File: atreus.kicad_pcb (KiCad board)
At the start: 2 copper layers, 139.7 x 101.6 mm, 45 parts

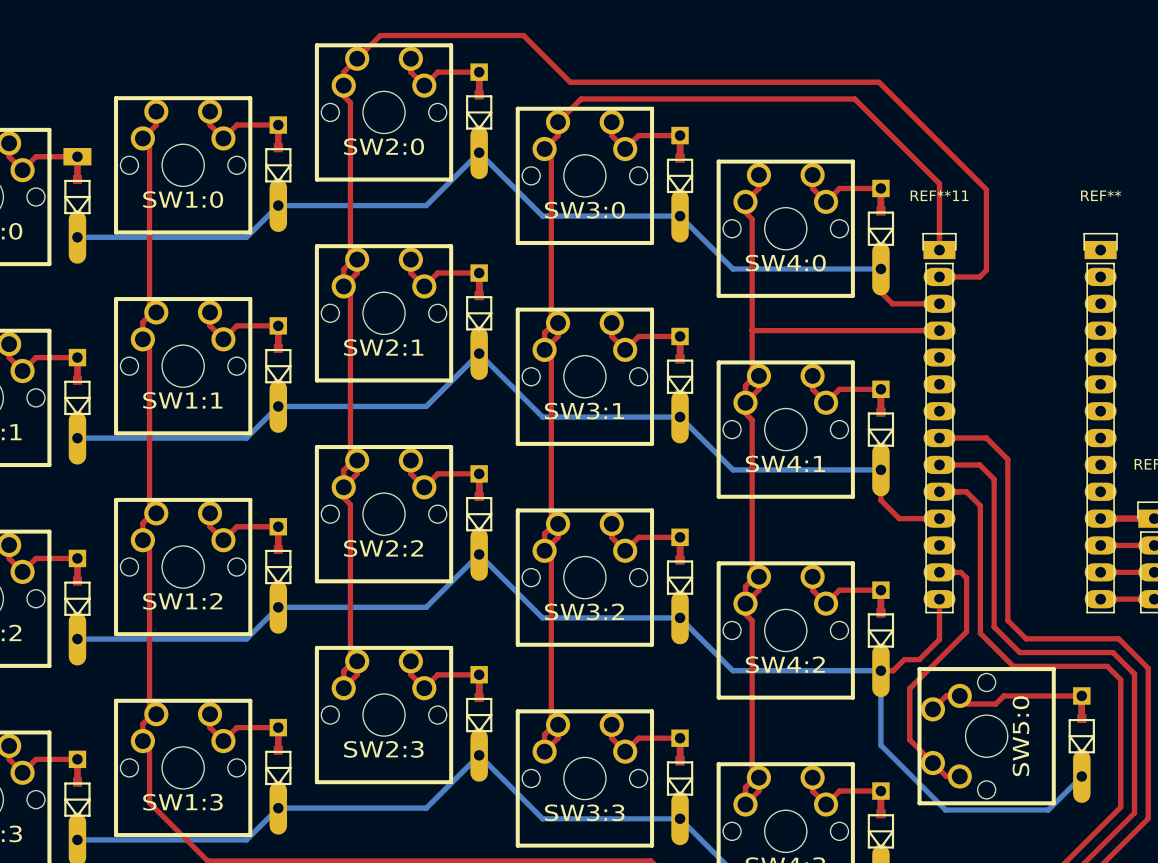
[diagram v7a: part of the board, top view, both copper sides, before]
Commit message: make diode pads bigger
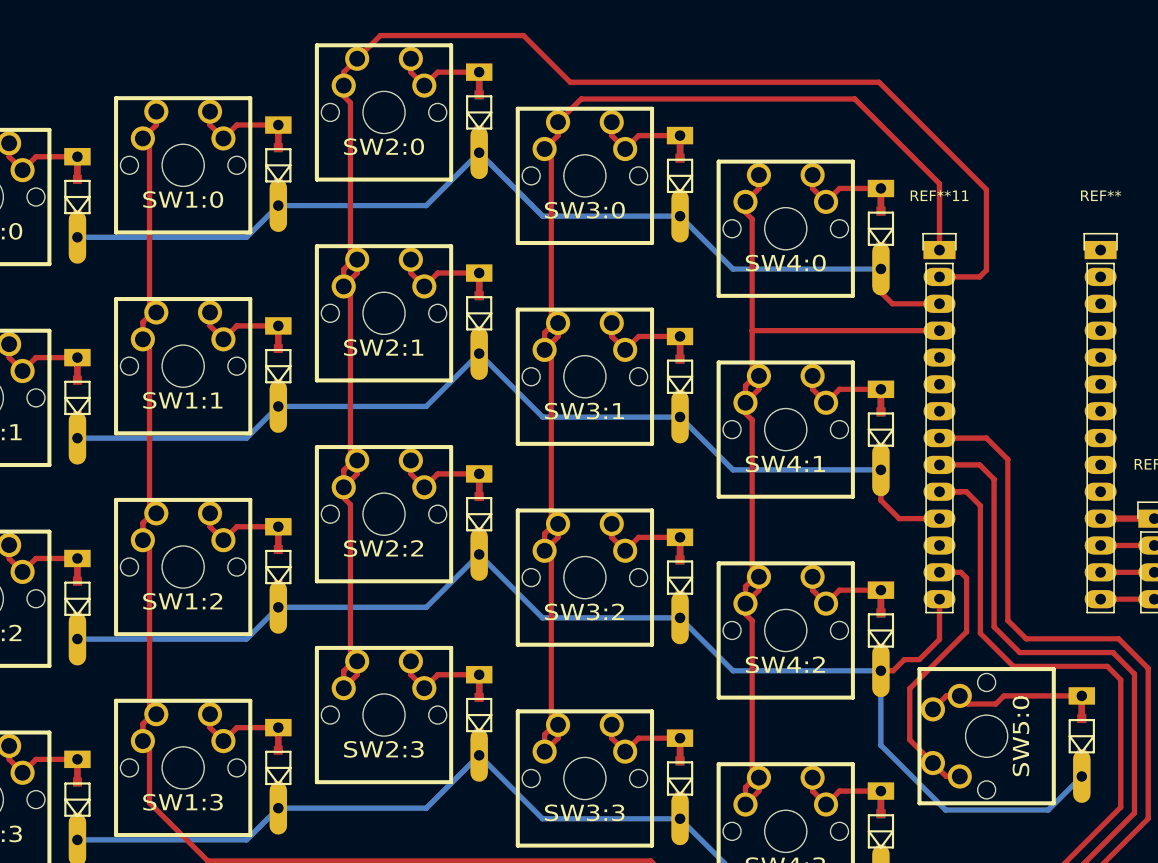
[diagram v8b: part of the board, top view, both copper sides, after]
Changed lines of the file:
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@@
     (mod_text_size 1.524 1.524)
     (mod_text_width 0.3048)
-    (pad_size 1.651 5)
+    (pad_size 2.5 1.651)
     (pad_drill 0.9906)
     (pad_to_mask_clearance 0.254)
@@
     (pad 1 thru_hole oval (at -3.81 0 180) (size 1.651 5) (drill 0.9906) (layers *.Cu *.SilkS *.Mask)
       (net 1 N-row-0))
-    (pad 2 thru_hole rect (at 3.81 0) (size 2.651 1.651) (drill 0.9906) (layers *.Cu *.SilkS *.Mask)
+    (pad 2 thru_hole rect (at 3.81 0) (size 2.5 1.651) (drill 0.9906) (layers *.Cu *.SilkS *.Mask)
       (net 11 N-diode-0))
     (pad 99 smd rect (at -1.6637 0) (size 0.8382 0.8382) (layers Front F.Paste F.Mask))
@@
     (pad 1 thru_hole oval (at -3.81 0 180) (size 1.651 5) (drill 0.9906) (layers *.Cu *.SilkS *.Mask)
       (net 2 N-row-1))
-    (pad 2 thru_hole rect (at 3.81 0) (size 1.651 1.651) (drill 0.9906) (layers *.Cu *.SilkS *.Mask)
+    (pad 2 thru_hole rect (at 3.81 0) (size 2.5 1.651) (drill 0.9906) (layers *.Cu *.SilkS *.Mask)
       (net 12 N-diode-1))
     (pad 99 smd rect (at -1.6637 0) (size 0.8382 0.8382) (layers Front F.Paste F.Mask))
@@
     (pad 1 thru_hole oval (at -3.81 0 180) (size 1.651 5) (drill 0.9906) (layers *.Cu *.SilkS *.Mask)
       (net 3 N-row-2))
-    (pad 2 thru_hole rect (at 3.81 0) (size 1.651 1.651) (drill 0.9906) (layers *.Cu *.SilkS *.Mask)
+    (pad 2 thru_hole rect (at 3.81 0) (size 2.5 1.651) (drill 0.9906) (layers *.Cu *.SilkS *.Mask)
       (net 13 N-diode-2))
     (pad 99 smd rect (at -1.6637 0) (size 0.8382 0.8382) (layers Front F.Paste F.Mask))
@@
     (pad 1 thru_hole oval (at -3.81 0 180) (size 1.651 5) (drill 0.9906) (layers *.Cu *.SilkS *.Mask)
       (net 4 N-row-3))
-    (pad 2 thru_hole rect (at 3.81 0) (size 1.651 1.651) (drill 0.9906) (layers *.Cu *.SilkS *.Mask)
+    (pad 2 thru_hole rect (at 3.81 0) (size 2.5 1.651) (drill 0.9906) (layers *.Cu *.SilkS *.Mask)
       (net 14 N-diode-3))
     (pad 99 smd rect (at -1.6637 0) (size 0.8382 0.8382) (layers Front F.Paste F.Mask))
@@
     (pad 1 thru_hole oval (at -3.81 0 180) (size 1.651 5) (drill 0.9906) (layers *.Cu *.SilkS *.Mask)
       (net 1 N-row-0))
-    (pad 2 thru_hole rect (at 3.81 0) (size 1.651 1.651) (drill 0.9906) (layers *.Cu *.SilkS *.Mask)
+    (pad 2 thru_hole rect (at 3.81 0) (size 2.5 1.651) (drill 0.9906) (layers *.Cu *.SilkS *.Mask)
       (net 15 N-diode-4))
     (pad 99 smd rect (at -1.6637 0) (size 0.8382 0.8382) (layers Front F.Paste F.Mask))
@@
     (pad 1 thru_hole oval (at -3.81 0 180) (size 1.651 5) (drill 0.9906) (layers *.Cu *.SilkS *.Mask)
       (net 2 N-row-1))
-    (pad 2 thru_hole rect (at 3.81 0) (size 1.651 1.651) (drill 0.9906) (layers *.Cu *.SilkS *.Mask)
+    (pad 2 thru_hole rect (at 3.81 0) (size 2.5 1.651) (drill 0.9906) (layers *.Cu *.SilkS *.Mask)
       (net 16 N-diode-5))
     (pad 99 smd rect (at -1.6637 0) (size 0.8382 0.8382) (layers Front F.Paste F.Mask))
@@
     (pad 1 thru_hole oval (at -3.81 0 180) (size 1.651 5) (drill 0.9906) (layers *.Cu *.SilkS *.Mask)
       (net 3 N-row-2))
-    (pad 2 thru_hole rect (at 3.81 0) (size 1.651 1.651) (drill 0.9906) (layers *.Cu *.SilkS *.Mask)
+    (pad 2 thru_hole rect (at 3.81 0) (size 2.5 1.651) (drill 0.9906) (layers *.Cu *.SilkS *.Mask)
       (net 17 N-diode-6))
     (pad 99 smd rect (at -1.6637 0) (size 0.8382 0.8382) (layers Front F.Paste F.Mask))
@@
     (pad 1 thru_hole oval (at -3.81 0 180) (size 1.651 5) (drill 0.9906) (layers *.Cu *.SilkS *.Mask)
       (net 4 N-row-3))
-    (pad 2 thru_hole rect (at 3.81 0) (size 1.651 1.651) (drill 0.9906) (layers *.Cu *.SilkS *.Mask)
+    (pad 2 thru_hole rect (at 3.81 0) (size 2.5 1.651) (drill 0.9906) (layers *.Cu *.SilkS *.Mask)
       (net 18 N-diode-7))
     (pad 99 smd rect (at -1.6637 0) (size 0.8382 0.8382) (layers Front F.Paste F.Mask))
@@
     (pad 1 thru_hole oval (at -3.81 0 180) (size 1.651 5) (drill 0.9906) (layers *.Cu *.SilkS *.Mask)
       (net 1 N-row-0))
-    (pad 2 thru_hole rect (at 3.81 0) (size 1.651 1.651) (drill 0.9906) (layers *.Cu *.SilkS *.Mask)
+    (pad 2 thru_hole rect (at 3.81 0) (size 2.5 1.651) (drill 0.9906) (layers *.Cu *.SilkS *.Mask)
       (net 19 N-diode-8))
     (pad 99 smd rect (at -1.6637 0) (size 0.8382 0.8382) (layers Front F.Paste F.Mask))
@@
     (pad 1 thru_hole oval (at -3.81 0 180) (size 1.651 5) (drill 0.9906) (layers *.Cu *.SilkS *.Mask)
       (net 2 N-row-1))
-    (pad 2 thru_hole rect (at 3.81 0) (size 1.651 1.651) (drill 0.9906) (layers *.Cu *.SilkS *.Mask)
+    (pad 2 thru_hole rect (at 3.81 0) (size 2.5 1.651) (drill 0.9906) (layers *.Cu *.SilkS *.Mask)
       (net 20 N-diode-9))
     (pad 99 smd rect (at -1.6637 0) (size 0.8382 0.8382) (layers Front F.Paste F.Mask))
@@
     (pad 1 thru_hole oval (at -3.81 0 180) (size 1.651 5) (drill 0.9906) (layers *.Cu *.SilkS *.Mask)
       (net 3 N-row-2))
-    (pad 2 thru_hole rect (at 3.81 0) (size 1.651 1.651) (drill 0.9906) (layers *.Cu *.SilkS *.Mask)
+    (pad 2 thru_hole rect (at 3.81 0) (size 2.5 1.651) (drill 0.9906) (layers *.Cu *.SilkS *.Mask)
       (net 21 N-diode-10))
     (pad 99 smd rect (at -1.6637 0) (size 0.8382 0.8382) (layers Front F.Paste F.Mask))
@@
     (pad 1 thru_hole oval (at -3.81 0 180) (size 1.651 5) (drill 0.9906) (layers *.Cu *.SilkS *.Mask)
       (net 4 N-row-3))
-    (pad 2 thru_hole rect (at 3.81 0) (size 1.651 1.651) (drill 0.9906) (layers *.Cu *.SilkS *.Mask)
+    (pad 2 thru_hole rect (at 3.81 0) (size 2.5 1.651) (drill 0.9906) (layers *.Cu *.SilkS *.Mask)
       (net 22 N-diode-11))
     (pad 99 smd rect (at -1.6637 0) (size 0.8382 0.8382) (layers Front F.Paste F.Mask))
@@
     (pad 1 thru_hole oval (at -3.81 0 180) (size 1.651 5) (drill 0.9906) (layers *.Cu *.SilkS *.Mask)
       (net 1 N-row-0))
-    (pad 2 thru_hole rect (at 3.81 0) (size 1.651 1.651) (drill 0.9906) (layers *.Cu *.SilkS *.Mask)
+    (pad 2 thru_hole rect (at 3.81 0) (size 2.5 1.651) (drill 0.9906) (layers *.Cu *.SilkS *.Mask)
       (net 23 N-diode-12))
     (pad 99 smd rect (at -1.6637 0) (size 0.8382 0.8382) (layers Front F.Paste F.Mask))
@@
     (pad 1 thru_hole oval (at -3.81 0 180) (size 1.651 5) (drill 0.9906) (layers *.Cu *.SilkS *.Mask)
       (net 2 N-row-1))
-    (pad 2 thru_hole rect (at 3.81 0) (size 1.651 1.651) (drill 0.9906) (layers *.Cu *.SilkS *.Mask)
+    (pad 2 thru_hole rect (at 3.81 0) (size 2.5 1.651) (drill 0.9906) (layers *.Cu *.SilkS *.Mask)
       (net 24 N-diode-13))
     (pad 99 smd rect (at -1.6637 0) (size 0.8382 0.8382) (layers Front F.Paste F.Mask))
@@
     (pad 1 thru_hole oval (at -3.81 0 180) (size 1.651 5) (drill 0.9906) (layers *.Cu *.SilkS *.Mask)
       (net 3 N-row-2))
-    (pad 2 thru_hole rect (at 3.81 0) (size 1.651 1.651) (drill 0.9906) (layers *.Cu *.SilkS *.Mask)
+    (pad 2 thru_hole rect (at 3.81 0) (size 2.5 1.651) (drill 0.9906) (layers *.Cu *.SilkS *.Mask)
       (net 25 N-diode-14))
     (pad 99 smd rect (at -1.6637 0) (size 0.8382 0.8382) (layers Front F.Paste F.Mask))
@@
     (pad 1 thru_hole oval (at -3.81 0 180) (size 1.651 5) (drill 0.9906) (layers *.Cu *.SilkS *.Mask)
       (net 4 N-row-3))
-    (pad 2 thru_hole rect (at 3.81 0) (size 1.651 1.651) (drill 0.9906) (layers *.Cu *.SilkS *.Mask)
+    (pad 2 thru_hole rect (at 3.81 0) (size 2.5 1.651) (drill 0.9906) (layers *.Cu *.SilkS *.Mask)
       (net 26 N-diode-15))
     (pad 99 smd rect (at -1.6637 0) (size 0.8382 0.8382) (layers Front F.Paste F.Mask))
@@
     (pad 1 thru_hole oval (at -3.81 0 180) (size 1.651 5) (drill 0.9906) (layers *.Cu *.SilkS *.Mask)
       (net 1 N-row-0))
-    (pad 2 thru_hole rect (at 3.81 0) (size 1.651 1.651) (drill 0.9906) (layers *.Cu *.SilkS *.Mask)
+    (pad 2 thru_hole rect (at 3.81 0) (size 2.5 1.651) (drill 0.9906) (layers *.Cu *.SilkS *.Mask)
       (net 27 N-diode-16))
     (pad 99 smd rect (at -1.6637 0) (size 0.8382 0.8382) (layers Front F.Paste F.Mask))
@@
     (pad 1 thru_hole oval (at -3.81 0 180) (size 1.651 5) (drill 0.9906) (layers *.Cu *.SilkS *.Mask)
       (net 2 N-row-1))
-    (pad 2 thru_hole rect (at 3.81 0) (size 1.651 1.651) (drill 0.9906) (layers *.Cu *.SilkS *.Mask)
+    (pad 2 thru_hole rect (at 3.81 0) (size 2.5 1.651) (drill 0.9906) (layers *.Cu *.SilkS *.Mask)
       (net 28 N-diode-17))
     (pad 99 smd rect (at -1.6637 0) (size 0.8382 0.8382) (layers Front F.Paste F.Mask))
@@
     (pad 1 thru_hole oval (at -3.81 0 180) (size 1.651 5) (drill 0.9906) (layers *.Cu *.SilkS *.Mask)
       (net 3 N-row-2))
-    (pad 2 thru_hole rect (at 3.81 0) (size 1.651 1.651) (drill 0.9906) (layers *.Cu *.SilkS *.Mask)
+    (pad 2 thru_hole rect (at 3.81 0) (size 2.5 1.651) (drill 0.9906) (layers *.Cu *.SilkS *.Mask)
       (net 29 N-diode-18))
     (pad 99 smd rect (at -1.6637 0) (size 0.8382 0.8382) (layers Front F.Paste F.Mask))
@@
     (pad 1 thru_hole oval (at -3.81 0 180) (size 1.651 5) (drill 0.9906) (layers *.Cu *.SilkS *.Mask)
       (net 4 N-row-3))
-    (pad 2 thru_hole rect (at 3.81 0) (size 1.651 1.651) (drill 0.9906) (layers *.Cu *.SilkS *.Mask)
+    (pad 2 thru_hole rect (at 3.81 0) (size 2.5 1.651) (drill 0.9906) (layers *.Cu *.SilkS *.Mask)
       (net 30 N-diode-19))
     (pad 99 smd rect (at -1.6637 0) (size 0.8382 0.8382) (layers Front F.Paste F.Mask))
@@
     (pad 1 thru_hole oval (at -3.81 0 180) (size 1.651 5) (drill 0.9906) (layers *.Cu *.SilkS *.Mask)
       (net 3 N-row-2))
-    (pad 2 thru_hole rect (at 3.81 0) (size 1.651 1.651) (drill 0.9906) (layers *.Cu *.SilkS *.Mask)
+    (pad 2 thru_hole rect (at 3.81 0) (size 2.5 1.651) (drill 0.9906) (layers *.Cu *.SilkS *.Mask)
       (net 31 N-diode-20))
     (pad 99 smd rect (at -1.6637 0) (size 0.8382 0.8382) (layers Front F.Paste F.Mask))
